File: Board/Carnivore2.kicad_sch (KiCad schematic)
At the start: 132 parts, among them J1 Conn_01x02_Pin, J2 Conn_01x03_Pin, U7 50 MHz, X1 EDGE50/MSX, X2 HEADER_5X2, X3 HEADER_5X2

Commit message: Updated more footprints 3D view complete
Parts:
- AX1, AX2: value {Value} -> SJ1-3523N
- B1: value BAT -> BAT 3V; ALTIUM_VALUE 3v -> (none)
- C1, C2, C22, C3, C4: value 10mk -> 10uF 16V; footprint Library:C_1812_1 -> Capacitor_Tantalum_SMD:CP_EIA-3216-10_Kemet-I_Pad1.58x1.35mm_HandSolder; ALTIUM_VALUE 10uF 16v -> (none); DESCRIPTION Radial Polarized Capacitor -> (none)
- C10, C11, C12, C13, C14, C15, C16, C17, C30, C5, C6, C7, C8, C9: value 0.1mk -> 100nF; footprint Library:C_0603_1 -> Capacitor_SMD:C_0603_1608Metric; ALTIUM_VALUE 0.1 -> (none)
- C101, C102, C104, C201, C204, C24, C25, C27, C31, C32, C33, C34, C35, C36: footprint Library:C_0603_1 -> Capacitor_SMD:C_0603_1608Metric
- C103, C105, C203, C205: footprint Library:C_1206_1 -> Capacitor_Tantalum_SMD:CP_EIA-3216-10_Kemet-I_Pad1.58x1.35mm_HandSolder
- C23, C26, C29: footprint Library:C_1812_1 -> Capacitor_Tantalum_SMD:CP_EIA-3216-10_Kemet-I_Pad1.58x1.35mm_HandSolder
- C28: value 10uF 16v -> 10uF 16V; footprint Library:C_1812_1 -> Capacitor_Tantalum_SMD:CP_EIA-3216-10_Kemet-I_Pad1.58x1.35mm_HandSolder; DESCRIPTION Radial Polarized Capacitor -> (none)
- D1, D2: value D9 -> 1N4148; footprint Library:DIODE_1N4148_1 -> Diode_THT:D_DO-35_SOD27_P7.62mm_Horizontal; COMPONENTFIELD6 Published 8-Jun-2000 -> (none); DESCRIPTION Default Diode -> (none); ORIGINALNAME DIODE -> (none)
- D3, D4: footprint Library:DIODE_1N4148_1 -> Diode_THT:D_DO-35_SOD27_P7.62mm_Horizontal; COMPONENTFIELD6 Published 8-Jun-2000 -> (none); DESCRIPTION Default Diode -> (none); ORIGINALNAME DIODE -> (none)
- LED1: value ~ -> 150060YS75000; footprint Library:C_0603_1 -> LED_SMD:LED_0603_1608Metric_Pad1.05x0.95mm_HandSolder
- R10, R11, R12, R13, R14, R15, R16, R17, R18, R19, R2, R20, R21, R22, R23, R24, R25, R26, R27, R28, R29, R3, R30, R31, R32, R33, R34, R35, R36, R37, R38, R39, R4, R40, R41, R42, R5, R6, R7, R8, R9: value 331 -> 330E; footprint Library:R_0603_1 -> Resistor_SMD:R_0603_1608Metric; ALTIUM_VALUE 330 -> (none)
- R103, R203: footprint Library:R_0603_1 -> Resistor_SMD:R_0603_1608Metric; ALTIUM_VALUE 4k7 -> (none)
- R104, R204, R49, R60, R61: value 470 -> 470E; footprint Library:R_0603_1 -> Resistor_SMD:R_0603_1608Metric
- R43, R44, R64: value 10 -> 10E; footprint Library:R_0603_1 -> Resistor_SMD:R_0603_1608Metric; ALTIUM_VALUE 10 -> (none)
- R45: value 220 -> 220E; footprint Library:R_0603_1 -> Resistor_SMD:R_0603_1608Metric; ALTIUM_VALUE 220 -> (none)
- R46, R47, R48, R50, R66: footprint Library:R_0603_1 -> Resistor_SMD:R_0603_1608Metric; ALTIUM_VALUE 10k -> (none)
- R51, R58, R59: footprint Library:R_0603_1 -> Resistor_SMD:R_0603_1608Metric; ALTIUM_VALUE 1k -> (none)
- R57: value 1K -> 1k; footprint Library:R_0603_1 -> Resistor_SMD:R_0603_1608Metric; ALTIUM_VALUE 1k -> (none)
- R99: value 10 -> 0E; footprint Library:R_0603_1 -> Jumper:SolderJumper-2_P1.3mm_Bridged_Pad1.0x1.5mm; ALTIUM_VALUE 10 -> (none)
- U1: value ~ -> EP2C8Q208C8N; footprint Library:EP2C5Q208C8_1 -> Package_QFP:PQFP-208_28x28mm_P0.5mm; ALTIUM_VALUE * -> (none); CODE_JEDEC MS-029-FA-1 -> (none); COMPONENTLINK1DESCBC Manufacturer Link -> (none); COMPONENTLINK2DESCA4 Handbook -> (none); COMPONENTLINK3DESCAC Packaging Specification -> (none); DATASHEETDOCUMENT ver2.0, Jul-2005 -> (none); DIGIKEY (none) -> 544-1671-ND; LATESTREVISIONDATE 18-Aug-2005 -> (none); LATESTREVISIONNOTE Component Description Changed. -> (none); PACKAGEDOCUMENT ver13.0, May-2005 -> (none); PACKAGEREFERENCE PQFP208 -> (none); PUBLISHED 4-Mar-2005 -> (none); PUBLISHER Altium Limited -> (none)
- U2: value ~ -> MX29LV640ETTI-70G; footprint Library:M29W320DXXXNXX_1 -> Package_SO:TSOP-I-48_18.4x12mm_P0.5mm; ALTIUM_VALUE * -> (none); DIGIKEY (none) -> 1092-1104-ND
- U3: value ~ -> RMLV1616AGSA-5S#KA0; footprint Library:CY62167DV30_1 -> Package_SO:TSOP-I-48_18.4x12mm_P0.5mm; ALTIUM_VALUE * -> (none); DIGIKEY (none) -> RMLV1616AGSA-5S2#KA0CT-ND
- U4: value ~ -> M25P80-VMN3TPB; CODE_IPC SO8 -> (none); CODE_JEDEC MS-012-AA -> (none); COMPONENTLINK1DESCBC Manufacturer Link -> (none); COMPONENTLINK1URL http://www.altera.com/products/devices/config/cfg-index.html -> (none); COMPONENTLINK2DESCA4 Configuration Handbook -> (none); COMPONENTLINK2URL http://www.altera.com/literature/hb/cfg/config_handbook.pdf -> (none); COMPONENTLINK3DESCAC Pinout Specification -> (none); COMPONENTLINK3URL http://www.altera.com/literature/hb/cfg/cyc_c51014.pdf -> (none); COMPONENTLINK4DESC94 Packaging Specification -> (none); COMPONENTLINK4URL http://www.altera.com/literature/ds/dspkg.pdf -> (none); CONFIGURES Cyclone II, Stratix II, & Cyclone Devices -> (none); DATASHEETDOCUMENT ver2.0, Oct-2003 -> (none); DIGIKEY (none) -> 1450-M25P80-VMN3TPBCT-ND; LATESTREVISIONDATE 6-Jun-2005 -> (none); LATESTREVISIONNOTE Stylized 3D Model Added. -> (none); PACKAGEDOCUMENT ver11.0, Feb-2003 -> (none); PACKAGEREFERENCE SOIC8 -> (none); PUBLISHED 17-Sep-2003 -> (none); PUBLISHER Altium Limited -> (none)
- U5: value ~ -> PCM5101APWR; DIGIKEY (none) -> 296-36706-1-ND
- U6: value ~ -> AT93C46DN-SH-T; ALTIUM_VALUE * -> (none); COMPONENTLINK1DESCBC Manufacturer Link -> (none); COMPONENTLINK1URL http://www.st.com/ -> (none); COMPONENTLINK2DESCA4 Datasheet -> (none); COMPONENTLINK2URL http://www.st.com/stonline/products/literature/ds/4997/m93c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 -> (none); DATASHEETDOCUMENT Feb-1999 -> (none); DIGIKEY (none) -> AT93C46DN-SH-TCT-ND; LATESTREVISIONDATE 6-Jun-2005 -> (none); LATESTREVISIONNOTE Stylized 3D Model Added. -> (none); PACKAGEDOCUMENT Jun-1998 -> (none); PACKAGEREFERENCE PSDIP8A -> (none); PUBLISHED 24-Aug-2001 -> (none); PUBLISHER Altium Limited -> (none)
- U7: value 50 MHz -> SG3225CAN 50.0000M-TJGA6; footprint Library:SG-310_1 -> Library:SG3225CAN; ALTIUM_VALUE 50 MHz -> (none); DIGIKEY (none) -> 114-SG3225CAN50.0000M-TJGA6CT-ND
- U9: value ~ -> PCM1808PWR; DIGIKEY (none) -> 296-26307-1-ND
- UCT1: value 1.2v -> AP2114HA-1.2TRG1; footprint Library:ADP3338_1 -> Package_TO_SOT_SMD:SOT-223; ALTIUM_VALUE 3.3 -> (none)
- UCT2, UCT3: value 3.3v -> AP2111H-3.3TRG1; footprint Library:ADP3338_1 -> Package_TO_SOT_SMD:SOT-223; ALTIUM_VALUE * -> (none)
- X1: ALTIUM_VALUE * -> (none)
- X2: value HEADER_5X2 -> 302-S101; ALTIUM_VALUE AS -> (none); DIGIKEY (none) -> ED1543-ND; LATESTREVISIONDATE 17-Jul-2002 -> (none); LATESTREVISIONNOTE Re-released for DXP Platform. -> (none); PUBLISHER Altium Limited -> (none)
- X3: value HEADER_5X2 -> 302-S101; ALTIUM_VALUE JTAG -> (none); DIGIKEY (none) -> ED1543-ND; LATESTREVISIONDATE 17-Jul-2002 -> (none); LATESTREVISIONNOTE Re-released for DXP Platform. -> (none); PUBLISHER Altium Limited -> (none)
- XC1: value ~ -> 101D-TAAB-R01; footprint Library:CF-50-001_1 -> Library:CF-Card_101D-TAAB-R01; COMPONENTLINK1DESCBC Manufacturer Link -> (none); COMPONENTLINK1URL http://www.3m.com/ -> (none); COMPONENTLINK2DESCA4 3M Interconnect -> (none); COMPONENTLINK2URL http://www.3M.com/us/electronics_mfg/interconnects/ -> (none); DATASHEETDOCUMENT May-2003 -> (none); DIGIKEY (none) -> 3M5455-ND; PACKAGEDOCUMENT May-2003 -> (none); PACKAGEREFERENCE N7E50-7516 -> (none); PADDIMENSIONS Follow nominal values. -> (none); PCB_LAYOUT Complies with manufacturer's recommendation. -> (none); PUBLISHED 6-Jun-2005 -> (none); PUBLISHER Altium Limited -> (none)
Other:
- note removed: "CF-CARD"
- moved on the sheet: C23, C25, J1, R47

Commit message: Some last details
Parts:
- added C18, C19, C20: 100nF, Capacitor_SMD:C_0603_1608Metric, symbol Sheet1-altium-import:root_1_C_0805
- AX1, AX2: DIGIKEY (none) -> CP1-3523N-ND
- C1, C105, C2, C205, C22, C23, C26, C28, C29, C3, C4: value 10uF 16V -> 10uF 10V; DIGIKEY (none) -> 399-3684-1-ND
- C10, C102, C11, C12, C13, C14, C15, C16, C17, C24, C25, C27, C30, C31, C32, C33, C34, C35, C5, C6, C7, C8, C9: DIGIKEY (none) -> 311-1088-1-ND
- C101, C201, C36: DIGIKEY (none) -> 490-1459-1-ND
- C103, C203: value 10uF 16V -> 1uF 10V; DIGIKEY (none) -> 399-9449-1-ND
- C104, C204: DIGIKEY (none) -> 1276-1134-1-ND
- D1, D2, D3, D4: DIGIKEY (none) -> 1N4148FSCT-ND
- LED1: DIGIKEY (none) -> 732-4981-1-ND
- R10, R11, R12, R13, R14, R15, R16, R17, R18, R19, R2, R20, R21, R22, R23, R24, R25, R26, R27, R28, R29, R3, R30, R31, R32, R33, R34, R35, R36, R37, R38, R39, R4, R40, R41, R42, R5, R6, R7, R8, R9: DIGIKEY (none) -> RMCF0603FT330RCT-ND
- R103, R203: value 4.7k -> 75E; DIGIKEY (none) -> RMCF0603FT75R0CT-ND
- R104, R204, R49, R60, R61: DIGIKEY (none) -> RMCF0603FT470RCT-ND
- R43, R44, R64: DIGIKEY (none) -> RMCF0603FT10R0CT-ND
- R45: DIGIKEY (none) -> RMCF0603FT220RCT-ND
- R46, R47, R48, R50, R66: DIGIKEY (none) -> RMCF0603FT10K0CT-ND
- R51, R57, R58, R59: DIGIKEY (none) -> RMCF0603FT1K00CT-ND
- UCT1: DIGIKEY (none) -> AP2114HA-1.2TRG1DICT-ND
- UCT2, UCT3: DIGIKEY (none) -> AP2111H-3.3TRG1DICT-ND
- X2, X3: footprint Library:HDR2X5 -> Library:302-S101
- XC1: DIGIKEY 3M5455-ND -> 4827-101D-TAAB-R01-ND
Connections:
- net GND: now also C18.2, C19.1, C20.2
- net VCC1.2: now also C18.1, C19.2, C20.1
- net VCC3.3A: now also C26.2 (PLUS), C27.2, U5.1 (CPVDD)
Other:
- moved on the sheet: C104, C204

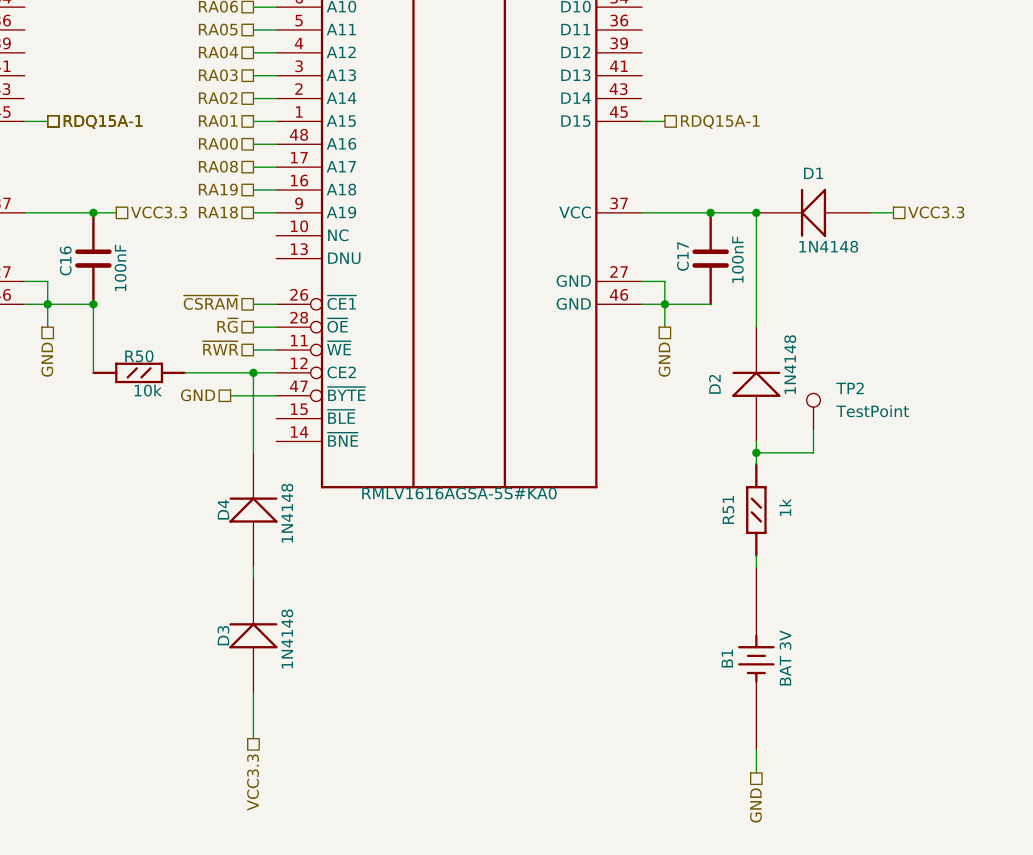
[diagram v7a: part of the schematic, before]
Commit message: Corrections in silkscreen for wrong direction of some capacitors and all diodes
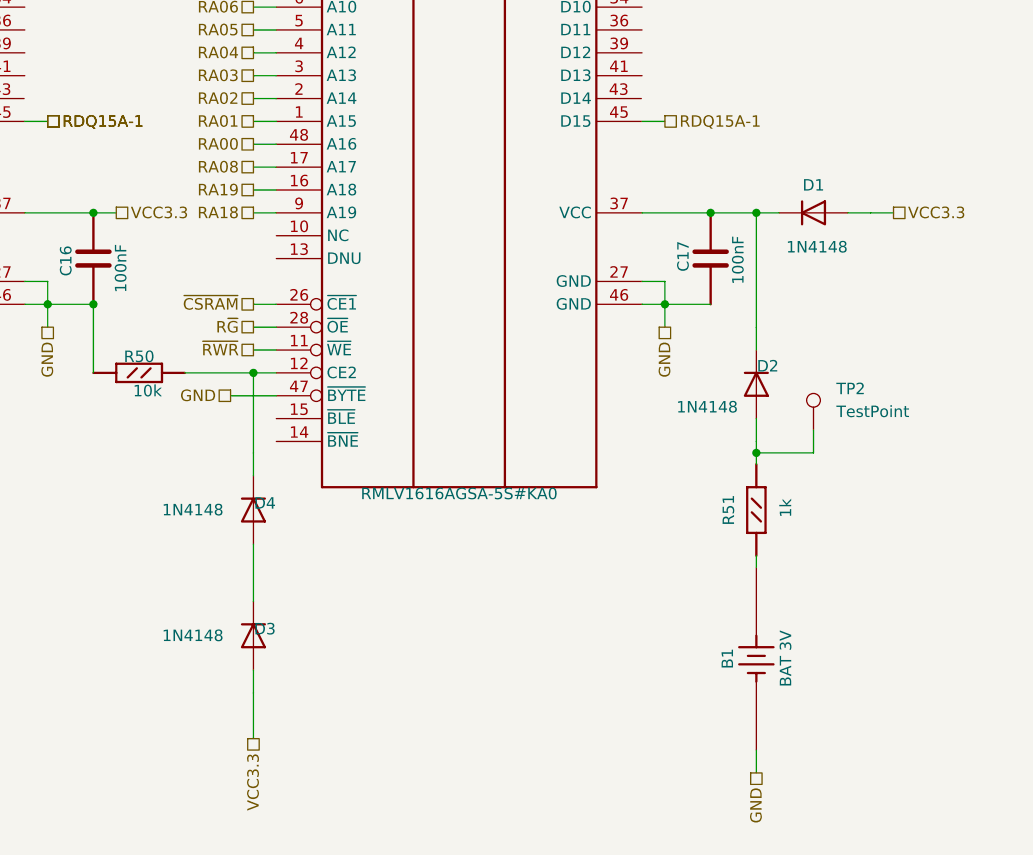
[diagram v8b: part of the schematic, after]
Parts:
- D1: symbol Sheet1-altium-import:root_2_DIODE -> Diode:1N4148
- D2, D3, D4: symbol Sheet1-altium-import:root_1_DIODE -> Diode:1N4148
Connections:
- net VCC3.3: now also D1.2 (A), D3.2 (A); no longer D1.1 (A), D3.1 (A)
- net at C17.1, U3.37 (VCC): now also D1.1 (K), D2.1 (K); no longer D1.2 (K), D2.2 (K)
- net at R50.1, U3.12 (CE2): now also D4.1 (K); no longer D4.2 (K)
- net at R51.1, TP2.1: now also D2.2 (A); no longer D2.1 (A)
- new net: D3.1 (K), D4.2 (A)
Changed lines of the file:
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@@
   (junction (at 285.115 36.195) (diameter 0) (color 0 0 0 0)
   )
-  (junction (at 226.06 133.35) (diameter 0) (color 0 0 0 0)
-  )
   (junction (at 523.24 72.39) (diameter 0) (color 0 0 0 0)
   )
@@
   (junction (at 452.12 232.41) (diameter 0) (color 0 0 0 0)
   )
+  (junction (at 226.06 133.35) (diameter 0) (color 0 0 0 0)
+  )
   (junction (at 406.4 227.33) (diameter 0) (color 0 0 0 0)
   )
@@
     (stroke (width 0.254) (type default))
   )
+  (wire (pts (xy 226.06 133.35) (xy 228.6 133.35))
+    (stroke (width 0) (type default))
+  )
   (wire (pts (xy 78.74 271.78) (xy 81.28 271.78))
     (stroke (width 0.254) (type default))
@@
     (stroke (width 0.254) (type default))
   )
+  (wire (pts (xy 170.18 184.15) (xy 170.18 186.69))
+    (stroke (width 0) (type default))
+  )
   (wire (pts (xy 91.44 335.28) (xy 93.98 335.28))
     (stroke (width 0.254) (type default))
@@
     (stroke (width 0.254) (type default))
   )
+  (wire (pts (xy 226.06 146.05) (xy 226.06 148.59))
+    (stroke (width 0) (type default))
+  )
   (wire (pts (xy 170.18 92.71) (xy 172.72 92.71))
     (stroke (width 0.254) (type default))
@@
     (stroke (width 0.254) (type default))
   )
+  (wire (pts (xy 170.18 160.02) (xy 170.18 162.56))
+    (stroke (width 0) (type default))
+  )
   (wire (pts (xy 267.97 41.91) (xy 267.97 44.45))
     (stroke (width 0) (type default))
@@
     (stroke (width 0) (type default))
   )
-  (wire (pts (xy 170.18 172.72) (xy 170.18 173.99))
+  (wire (pts (xy 170.18 170.18) (xy 170.18 176.53))
     (stroke (width 0) (type default))
   )
@@
     (stroke (width 0.254) (type default))
   )
+  (wire (pts (xy 226.06 156.21) (xy 226.06 158.75))
+    (stroke (width 0) (type default))
+  )
   (wire (pts (xy 313.055 61.595) (xy 313.055 43.815))
     (stroke (width 0) (type default))
@@
     (stroke (width 0.254) (type default))
   )
+  (wire (pts (xy 236.22 133.35) (xy 238.76 133.35))
+    (stroke (width 0) (type default))
+  )
   (wire (pts (xy 137.16 298.45) (xy 139.7 298.45))
     (stroke (width 0.254) (type default))
@@
     )
   )
-  (symbol (lib_id "Sheet1-altium-import:root_2_DIODE") (at 233.68 135.89 0) (unit 1)
+  (symbol (lib_id "Diode:1N4148") (at 232.41 133.35 0) (unit 1)
     (in_bom yes) (on_board yes) (dnp no)
-    (property "Reference" "D1" (at 232.41 128.27 0)
+    (property "Reference" "D1" (at 232.41 129.54 0)
       (effects (font (size 1.27 1.27)) (justify top))
     )
-    (property "Value" "1N4148" (at 237.49 137.16 0)
+    (property "Value" "1N4148" (at 236.22 137.16 0)
       (effects (font (size 1.27 1.27)) (justify right))
     )
-    (property "Footprint" "Diode_THT:D_DO-35_SOD27_P7.62mm_Horizontal" (at 233.68 135.89 0)
+    (property "Footprint" "Diode_THT:D_DO-35_SOD27_P7.62mm_Horizontal" (at 232.41 133.35 0)
       (effects (font (size 1.27 1.27)) hide)
     )
-    (property "Datasheet" "" (at 233.68 135.89 0)
+    (property "Datasheet" "https://assets.nexperia.com/documents/data-sheet/1N4148_1N4448.pdf" (at 232.41 133.35 0)
       (effects (font (size 1.27 1.27)) hide)
     )
-    (property "DIGIKEY" "1N4148FSCT-ND" (at 233.68 135.89 0)
+    (property "DIGIKEY" "1N4148FSCT-ND" (at 232.41 133.35 0)
+      (effects (font (size 1.27 1.27)) hide)
+    )
+    (property "Sim.Device" "D" (at 232.41 133.35 0)
+      (effects (font (size 1.27 1.27)) hide)
+    )
+    (property "Sim.Pins" "1=K 2=A" (at 232.41 133.35 0)
       (effects (font (size 1.27 1.27)) hide)
     )
@@
     )
   )
-  (symbol (lib_id "Sheet1-altium-import:root_1_DIODE") (at 167.64 167.64 0) (unit 1)
+  (symbol (lib_id "Diode:1N4148") (at 170.18 166.37 270) (unit 1)
     (in_bom yes) (on_board yes) (dnp no)
-    (property "Reference" "D4" (at 167.64 166.37 90)
+    (property "Reference" "D4" (at 171.45 166.37 90)
       (effects (font (size 1.27 1.27)) (justify bottom))
     )
-    (property "Value" "1N4148" (at 173.99 170.18 90)
+    (property "Value" "1N4148" (at 160.02 166.37 90)
       (effects (font (size 1.27 1.27)) (justify left))
     )
-    (property "Footprint" "Diode_THT:D_DO-35_SOD27_P7.62mm_Horizontal" (at 167.64 167.64 0)
+    (property "Footprint" "Diode_THT:D_DO-35_SOD27_P7.62mm_Horizontal" (at 170.18 166.37 0)
+      (effects (font (size 1.27 1.27)) hide)
+    )
+    (property "Datasheet" "https://assets.nexperia.com/documents/data-sheet/1N4148_1N4448.pdf" (at 170.18 166.37 0)
+      (effects (font (size 1.27 1.27)) hide)
+    )
+    (property "DIGIKEY" "1N4148FSCT-ND" (at 170.18 166.37 0)
       (effects (font (size 1.27 1.27)) hide)
     )
-    (property "Datasheet" "" (at 167.64 167.64 0)
+    (property "Sim.Device" "D" (at 170.18 166.37 0)
       (effects (font (size 1.27 1.27)) hide)
     )
-    (property "DIGIKEY" "1N4148FSCT-ND" (at 167.64 167.64 0)
+    (property "Sim.Pins" "1=K 2=A" (at 170.18 166.37 0)
       (effects (font (size 1.27 1.27)) hide)
     )
@@
     )
   )
-  (symbol (lib_id "Sheet1-altium-import:root_1_DIODE") (at 223.52 153.67 0) (unit 1)
+  (symbol (lib_id "Diode:1N4148") (at 226.06 152.4 270) (unit 1)
     (in_bom yes) (on_board yes) (dnp no)
-    (property "Reference" "D2" (at 222.25 152.4 90)
+    (property "Reference" "D2" (at 227.33 151.13 90)
       (effects (font (size 1.27 1.27)) (justify bottom))
     )
-    (property "Value" "1N4148" (at 229.87 153.67 90)
+    (property "Value" "1N4148" (at 217.17 154.94 90)
       (effects (font (size 1.27 1.27)) (justify left))
     )
-    (property "Footprint" "Diode_THT:D_DO-35_SOD27_P7.62mm_Horizontal" (at 223.52 153.67 0)
+    (property "Footprint" "Diode_THT:D_DO-35_SOD27_P7.62mm_Horizontal" (at 226.06 152.4 0)
       (effects (font (size 1.27 1.27)) hide)
     )
-    (property "Datasheet" "" (at 223.52 153.67 0)
+    (property "Datasheet" "https://assets.nexperia.com/documents/data-sheet/1N4148_1N4448.pdf" (at 226.06 152.4 0)
       (effects (font (size 1.27 1.27)) hide)
     )
-    (property "DIGIKEY" "1N4148FSCT-ND" (at 223.52 153.67 0)
+    (property "DIGIKEY" "1N4148FSCT-ND" (at 226.06 152.4 0)
+      (effects (font (size 1.27 1.27)) hide)
+    )
+    (property "Sim.Device" "D" (at 226.06 152.4 0)
+      (effects (font (size 1.27 1.27)) hide)
+    )
+    (property "Sim.Pins" "1=K 2=A" (at 226.06 152.4 0)
       (effects (font (size 1.27 1.27)) hide)
     )
@@
     )
   )
-  (symbol (lib_id "Sheet1-altium-import:root_1_DIODE") (at 167.64 181.61 0) (unit 1)
+  (symbol (lib_id "Diode:1N4148") (at 170.18 180.34 270) (unit 1)
     (in_bom yes) (on_board yes) (dnp no)
-    (property "Reference" "D3" (at 167.64 180.34 90)
+    (property "Reference" "D3" (at 171.45 180.34 90)
       (effects (font (size 1.27 1.27)) (justify bottom))
     )
-    (property "Value" "1N4148" (at 173.99 184.15 90)
+    (property "Value" "1N4148" (at 160.02 180.34 90)
       (effects (font (size 1.27 1.27)) (justify left))
     )
-    (property "Footprint" "Diode_THT:D_DO-35_SOD27_P7.62mm_Horizontal" (at 167.64 181.61 0)
+    (property "Footprint" "Diode_THT:D_DO-35_SOD27_P7.62mm_Horizontal" (at 170.18 180.34 0)
+      (effects (font (size 1.27 1.27)) hide)
+    )
+    (property "Datasheet" "https://assets.nexperia.com/documents/data-sheet/1N4148_1N4448.pdf" (at 170.18 180.34 0)
+      (effects (font (size 1.27 1.27)) hide)
+    )
+    (property "DIGIKEY" "1N4148FSCT-ND" (at 170.18 180.34 0)
       (effects (font (size 1.27 1.27)) hide)
     )
-    (property "Datasheet" "" (at 167.64 181.61 0)
+    (property "Sim.Device" "D" (at 170.18 180.34 0)
       (effects (font (size 1.27 1.27)) hide)
     )
-    (property "DIGIKEY" "1N4148FSCT-ND" (at 167.64 181.61 0)
+    (property "Sim.Pins" "1=K 2=A" (at 170.18 180.34 0)
       (effects (font (size 1.27 1.27)) hide)
     )
